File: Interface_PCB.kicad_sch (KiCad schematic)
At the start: 7 parts, among them IC1 STM32L412RBT6P, J1 USB_B, J2 AVR-JTAG-10, J3 Conn_01x04, J4 Conn_01x04, J5 Conn_01x04, J6 Conn_01x04

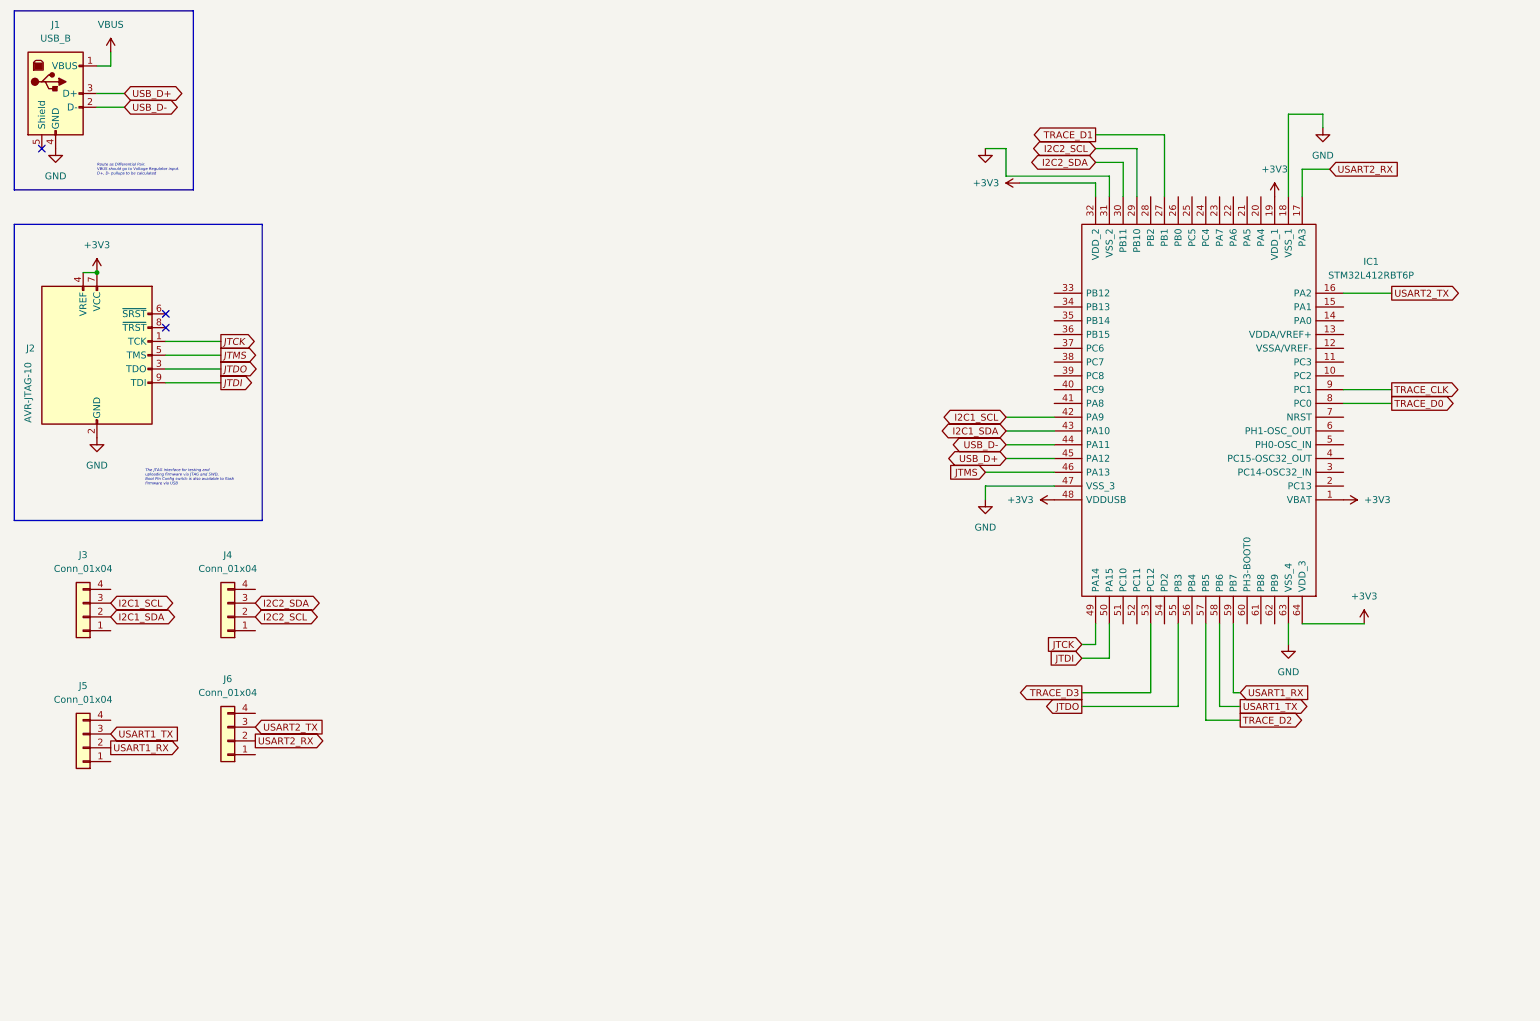
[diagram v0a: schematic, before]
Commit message: AMS connected
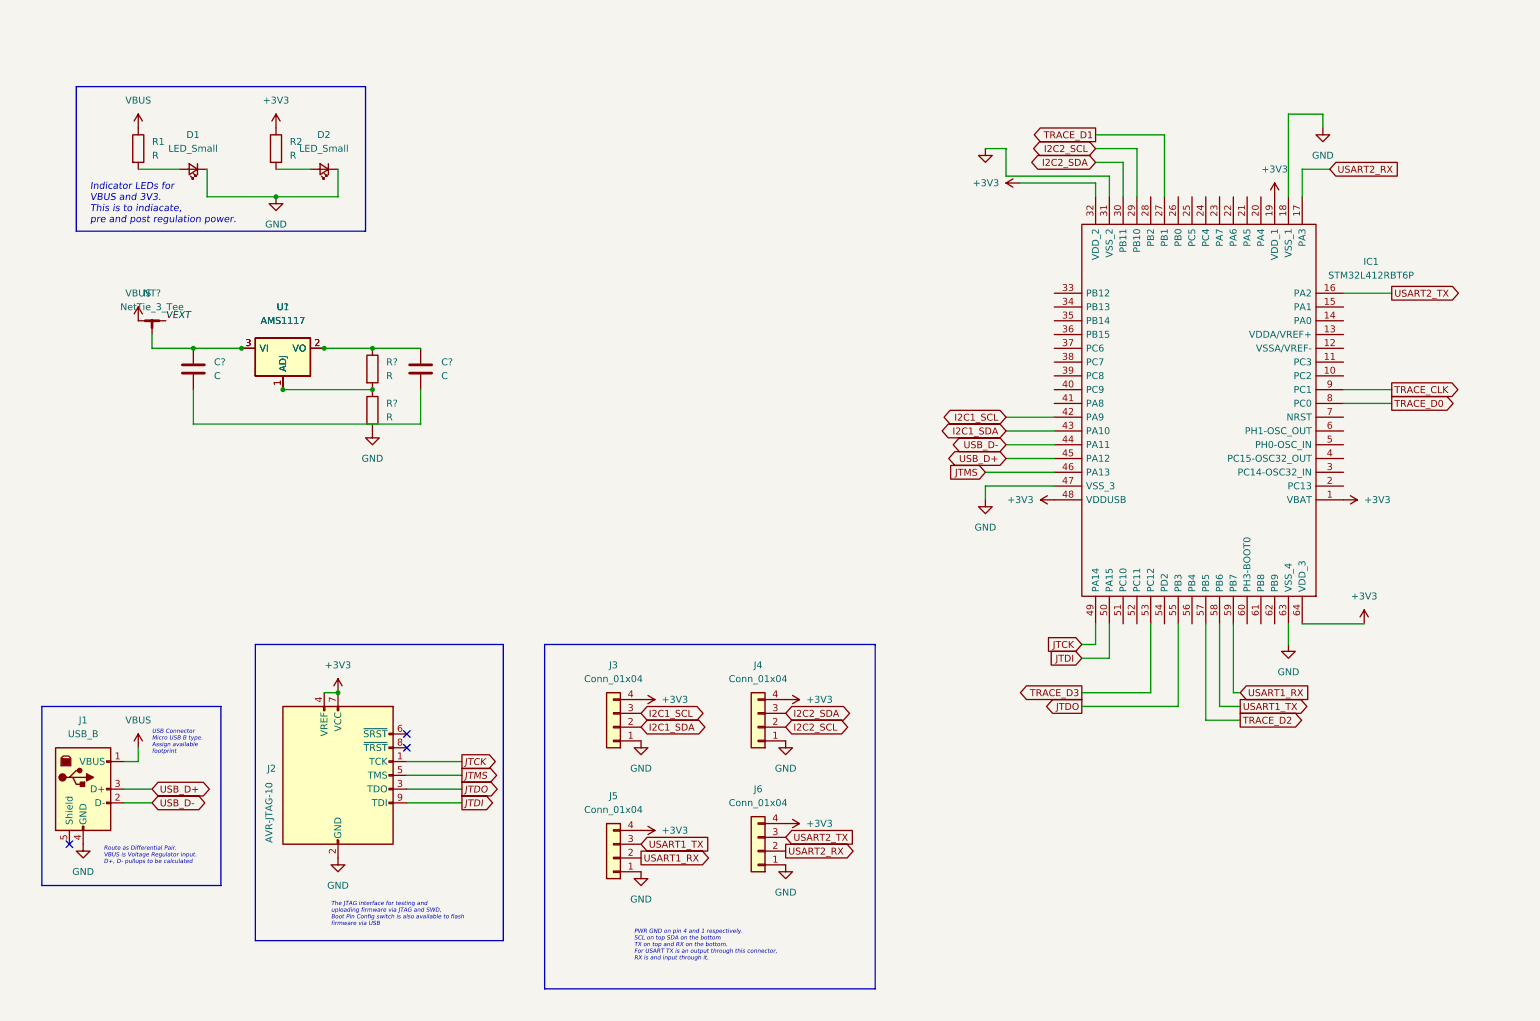
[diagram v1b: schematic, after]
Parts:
- added C? (x2): C, symbol Device:C
- added D1, D2: LED_Small, symbol Device:LED_Small
- added NT?: NetTie_3_Tee, symbol Device:NetTie_3_Tee
- added R1, R2, R? (x2): R, symbol Device:R
- added U1, U?: AMS1117, Package_TO_SOT_SMD:SOT-223-3_TabPin2, symbol Regulator_Linear:AMS1117
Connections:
- net +3V3: now also J3.4 (Pin_4), J4.4 (Pin_4), J5.4 (Pin_4), J6.4 (Pin_4), R2.1
- net GND: now also J3.1 (Pin_1), J4.1 (Pin_1), J5.1 (Pin_1), J6.1 (Pin_1), D1.1 (K), D2.1 (K), R?.2
- net VBUS: now also NT?.1, R1.1
- new net: D2.2 (A), R2.2
- new net: C?.1, NT?.3, U1.3 (VI), U?.3 (VI)
- new net: C?.2, C?.2
- new net: C?.1, R?.1, U1.2 (VO), U?.2 (VO)
- new net: R?.1, R?.2, U1.1 (ADJ), U?.1 (ADJ)
- new net: D1.2 (A), R1.2
- new net VEXT: NT?.2
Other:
- note added: "Indicator LEDs for VBUS and 3V3. This is to indiacate, pre and post regulation power."
- note added: "PWR GND on pin 4 and 1 respectively. SCL on top SDA on the bottom TX on top and RX on the bottom. For USART TX is an output through this connector, RX is and input through it."
- note added: "Route as Differential Pair. VBUS is Voltage Regulator input. D+, D- pullups to be calculated"
- note added: "USB Connector Micro USB B type. Assign available footprint"
- note removed: "Route as Differential Pair. VBUS should go to Voltage Regulator input. D+, D- pullups to be calculated"
- moved on the sheet: J1, J2, J3, J4, J5, J6

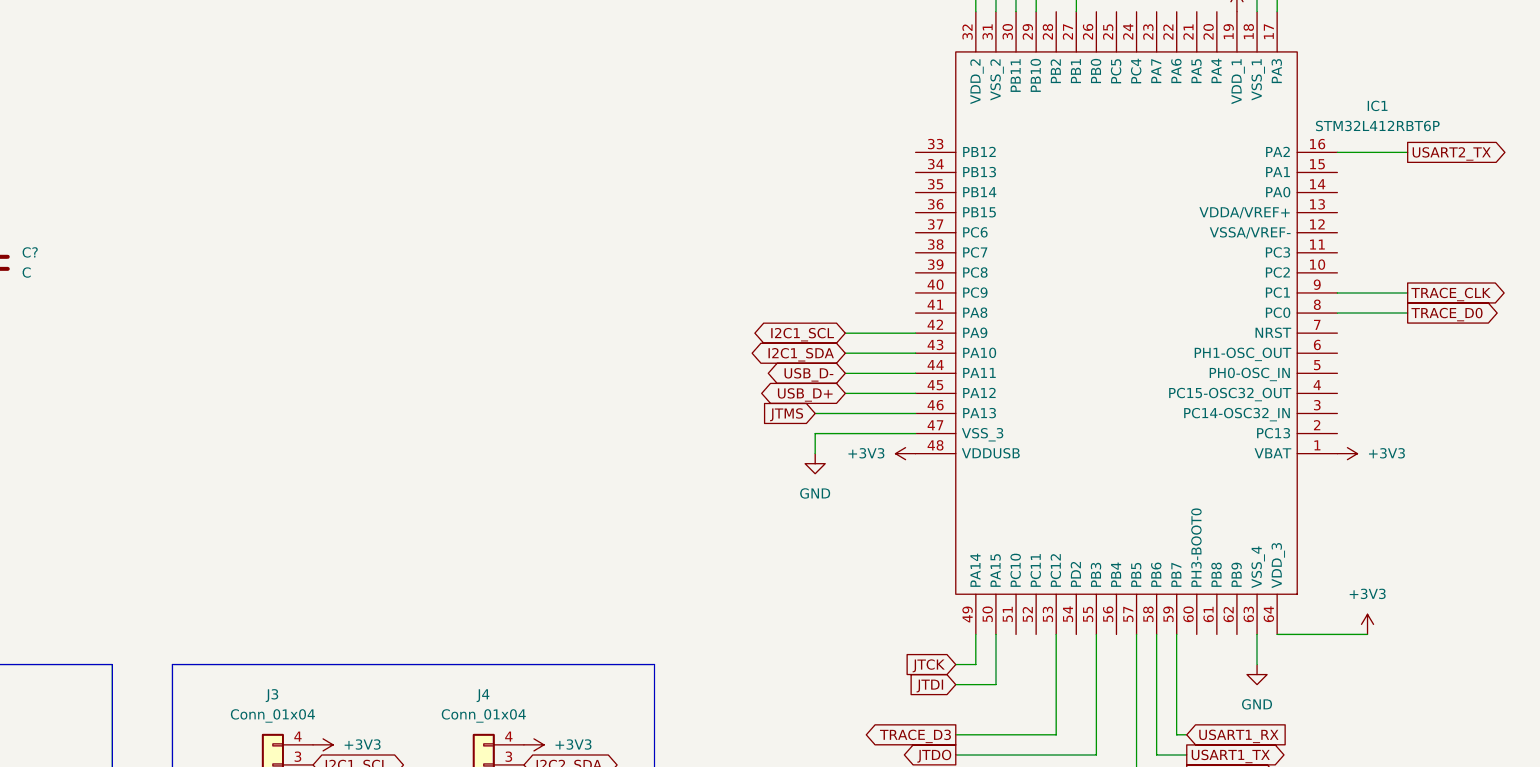
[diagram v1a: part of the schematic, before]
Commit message: Added crystal configs to schematic
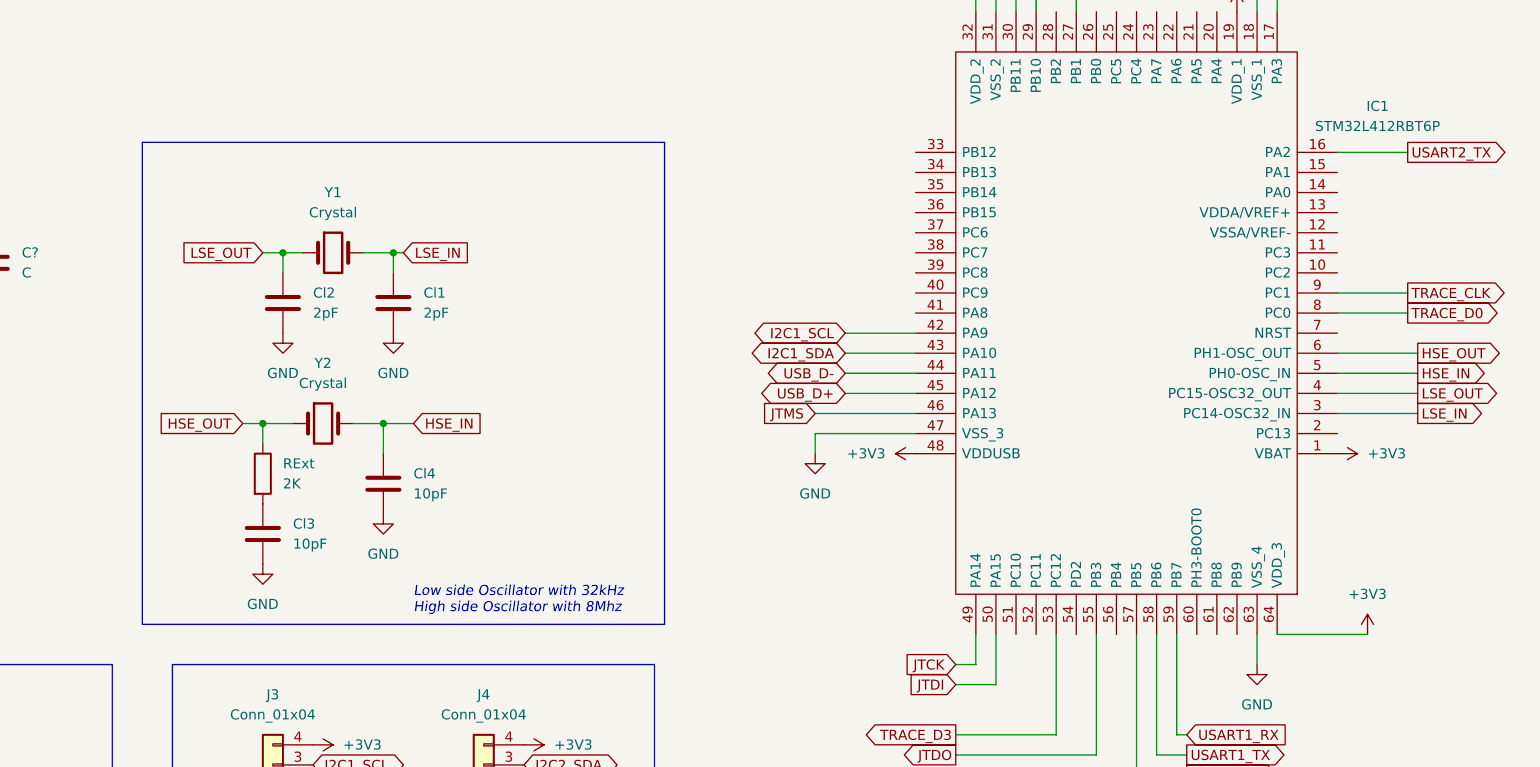
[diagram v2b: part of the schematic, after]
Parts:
- added Cl1, Cl2: 2pF, symbol Device:C
- added Cl3, Cl4: 10pF, symbol Device:C
- added RExt: 2K, symbol Device:R
- added Y1: Crystal, SamacSys_Parts:ABS05W32768KHZD2T, symbol Device:Crystal
- added Y2: Crystal, SamacSys_Parts:ECS80830QVSTR, symbol Device:Crystal
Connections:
- net GND: now also Cl1.2, Cl2.2, Cl3.2, Cl4.2
- net LSE_IN: now reaches IC1.3 (PC14-OSC32_IN)
- net LSE_IN: now also Cl1.1, Y1.2
- net LSE_OUT: now reaches IC1.4 (PC15-OSC32_OUT)
- net LSE_OUT: now also Cl2.1, Y1.1
- net HSE_IN: now reaches IC1.5 (PH0-OSC_IN)
- net HSE_IN: now also Cl4.1, Y2.2
- net HSE_OUT: now reaches IC1.6 (PH1-OSC_OUT)
- net HSE_OUT: now also RExt.1, Y2.1
- new net: Cl3.1, RExt.2
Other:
- note added: "Low side Oscillator with 32kHz High side Oscillator with 8Mhz"

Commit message: Final Schematic done, footprint assignment TBD
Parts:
- removed C? (x2): C, symbol Device:C
- removed NT?: NetTie_3_Tee, symbol Device:NetTie_3_Tee
- removed R? (x2): R, symbol Device:R
- removed U1, U?: AMS1117, Package_TO_SOT_SMD:SOT-223-3_TabPin2, symbol Regulator_Linear:AMS1117
- added C1, C2, C3: 22uF, symbol Device:C
- added C10, C11, C7, C8, C9: 100n, symbol Device:C
- added C12: 0.1uF, symbol Device:C
- added C4, C5: 10n, symbol Device:C
- added C6, CB1, CB2, CB3, CB4: 4.7u, symbol Device:C
- added C?: 1u, symbol Device:C
- added J7: Micro_SD_Card, Connector_Card:microSD_HC_Wuerth_693072010801, symbol Connector:Micro_SD_Card
- added L1, L?: 39nH, symbol Device:L
- added NT1: TEE, symbol Device:NetTie_3_Tee
- added U1: AMS1117-3.3, Package_TO_SOT_SMD:SOT-223-3_TabPin2, symbol Regulator_Linear:AMS1117-3.3
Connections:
- net +3V3: now also C10.1, C11.1, C4.1, C6.1, C7.1, C8.1, C9.1, C?.1, CB1.1, CB2.1, CB3.1, CB4.1, J7.4 (VDD), L?.1
- net GND: now also IC1.12 (VSSA/VREF-), C1.2, C10.2, C11.2, C12.2, C2.2, C3.2, C6.2, C7.2, C8.2, C9.2, CB1.2, CB2.2, CB3.2, CB4.2, J7.6 (VSS), U1.1 (GND)
- net HSE_OUT: no longer Y2.1
- net VBUS: now also NT1.1
- net VEXT: now also C1.1, L1.2
- net at Cl3.1, RExt.2: now also Y2.1
- net +3.3VA: now reaches IC1.13 (VDDA/VREF+)
- net +3.3VA: now also C5.1, L?.2
- net SPI1_CLK: now reaches IC1.15 (PA1)
- net SPI1_MISO: now reaches IC1.22 (PA6)
- net SPI1_MISO: now also J7.7 (DAT0)
- net SPI1_MOSI: now reaches IC1.23 (PA7)
- net SPI1_MOSI: now also J7.3 (CMD)
- new net: C3.1, U1.2 (VO)
- new net: C12.1, J7.9 (SHIELD)
- new net: C2.1, NT1.3, U1.3 (VI)
- new net: C4.2, C5.2, C?.2
- new net: L1.1, NT1.2
- new net CLK: J7.5 (CLK)
- new net CS: J7.2 (DAT3/CD)
- no-connect marks 3 -> 5
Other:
- note added: "?? check if reverse polarity protection is needed ??"
- note added: "Analog Power filter network. kept extra capacitor pad if required. filtering with a 39nH inductor."
- note added: "Fixed output LDO for 3.3 V rail. Input is through USB or external Power Pin. Probably should add footprint for either ferrite or inductor between VEXT and nettie."
- note added: "SD Card interfaced with SPI, add termination resistor if line is too long for low rise time."
- note added: "The 4.7uF capacitor is the Bulk decoupling capacitor. Place it close to the VDD VSS pins. The rest of the decoupling is through the other caps and pwr and gnd planes."
- moved on the sheet: Cl1, Cl2, Cl3, Cl4, D1, D2, IC1, J1, J2, J3, J4, J5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
